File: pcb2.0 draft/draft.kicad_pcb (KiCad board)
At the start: 2 copper layers, 13 parts, among them J3 Conn_01x04, J4 Conn_01x04, J5 Conn_01x04, U2 LM2576HVS-5, U3 LM2576HVS-3.3

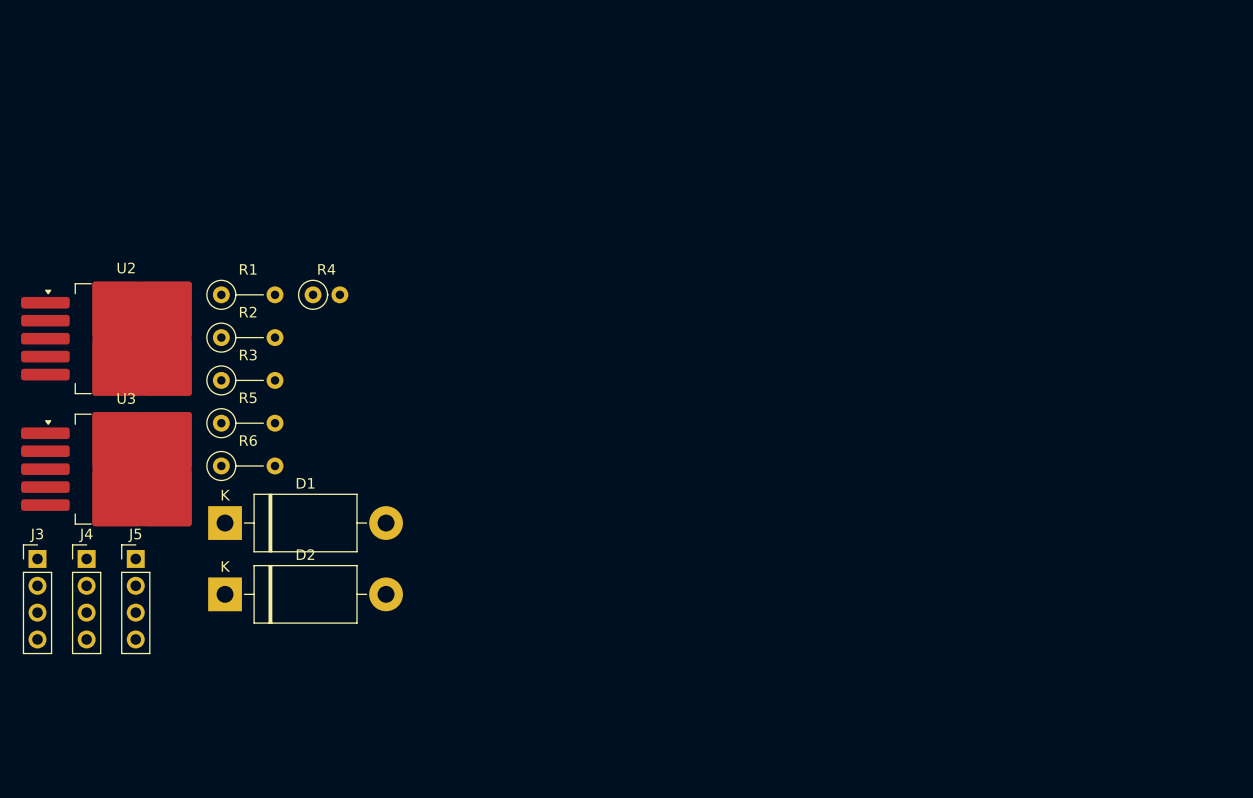
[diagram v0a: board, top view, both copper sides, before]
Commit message: completed pcb layout
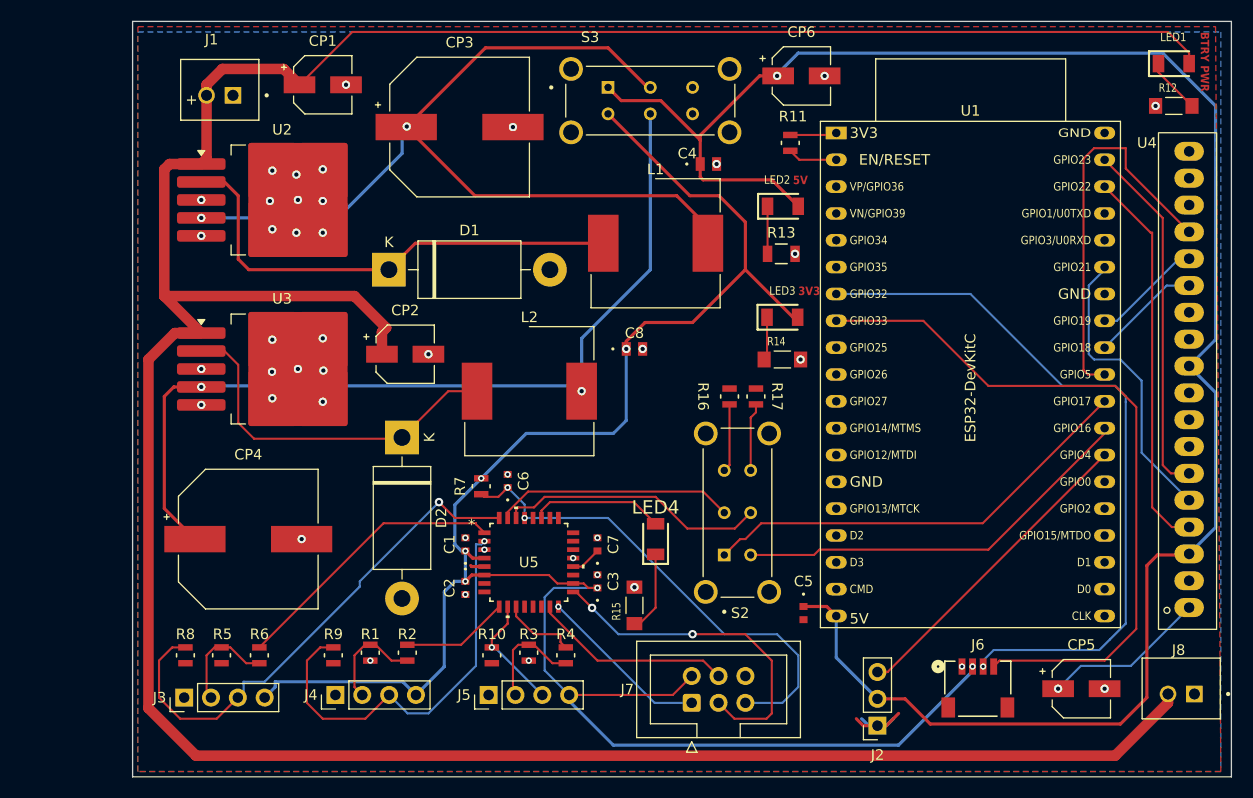
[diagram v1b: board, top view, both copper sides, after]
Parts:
- added C1: 0.1uF, cap_murata_0603:G-188_MUR-L, F.Cu at (137.0, 97.0)
- added C2: 0.1uF, cap_murata_0603:G-188_MUR-L, F.Cu at (137.0, 101.1)
- added C3: 0.1uF, cap_murata_0603:G-188_MUR-L, F.Cu at (149.5, 100.5)
- added C4: 1uF, cap_murata_0805:CAP_GRM21_MUR-L, F.Cu at (160.0, 61.0)
- added C5: 0.1uF, cap_murata_0603:G-188_MUR-L, F.Cu at (169.0, 103.5)
- added C6: 0.1uF, cap_murata_0603:G-188_MUR-L, F.Cu at (141.0, 91.0)
- added C7: 0.1uF, cap_murata_0603:G-188_MUR-L, F.Cu at (149.5, 97.0)
- added C8: 1uF, cap_murata_0805:CAP_GRM21_MUR-L, F.Cu at (153.0, 78.5)
- added CP1: 100uF, WurthE:CP_Wurth_WCAP-PSLP-D5L5.5, F.Cu at (123.5, 53.5)
- added CP2: 100uF, WurthE:CP_Wurth_WCAP-PSLP-D5L5.5, F.Cu at (131.3, 79.0)
- added CP3: 1mF, WurthE:CP_Wurth_WCAP-ASLI-D12.5L14, F.Cu at (136.4, 57.5)
- added CP4: 1mF, WurthE:CP_Wurth_WCAP-ASLI-D12.5L14, F.Cu at (116.5, 96.5)
- added CP5: 100uF, WurthE:CP_Wurth_WCAP-PSLP-D5L5.5, F.Cu at (195.3, 110.7)
- added CP6: 10uF, WurthE:CP_Wurth_WCAP-PSLP-D5L5.8, F.Cu at (168.8, 52.7)
- added J1: BTRY IN, jst_xh:JST_B2B-XH-A, F.Cu at (113.8, 54.0)
- added J2: Servo Header, Connector_PinSocket_2.54mm:PinSocket_1x03_P2.54mm_Vertical, F.Cu at (176.0, 114.2)
- added J6: QUIIC, quiic_jst:CONN_SM04B-SRSS-TB_JST, F.Cu at (185.5, 110.7)
- added J7: AVR-ISP-6, Connector_IDC:IDC-Header_2x03_P2.54mm_Vertical, F.Cu at (158.4, 112.0)
- added J8: BTRY OUT, jst_xh:JST_B2B-XH-A, F.Cu at (204.8, 110.6)
- added L1: 100uH, WE-PD:L_Wurth_WE-PD-1245, F.Cu at (155.0, 68.5)
- added L2: 100uH, WE-PD:L_Wurth_WE-PD-1245, F.Cu at (143.1, 82.5)
- added LED1: EAST3215BA3, led_smd_1206:LEDC3215X110N, F.Cu at (204.1, 51.5)
- added LED2: EAST3215BA3, led_smd_1206:LEDC3215X110N, F.Cu at (167.1, 65.0)
- added LED3: EAST3215BA3, led_smd_1206:LEDC3215X110N, F.Cu at (167.0, 75.5)
- added LED4: EAST3215BA3, led_smd_1206:LEDC3215X110N, F.Cu at (155.0, 96.5)
- added R10: 10k, R_SMD:RES_CR0805_VEN-L, F.Cu at (139.5, 107.5)
- added R11: 10k, R_SMD:RES_CR0805_VEN-L, F.Cu at (167.8, 59.0)
- added R12: 1.2k, r_erj_1p2k:RES_ERJU08J122V, F.Cu at (204.1, 55.5)
- added R13: 620, R_ERJ_620_1206:RC1206N_PAN-L, F.Cu at (166.9, 69.5)
- added R14: 270, r_erj_270:RES_ERJU08J271V, F.Cu at (167.0, 79.5)
- added R15: 270, r_erj_270:RES_ERJU08J271V, F.Cu at (153.0, 102.8)
- added R16: 10k, R_SMD:RES_CR0805_VEN-L, F.Cu at (162.0, 83.0)
- added R17: 10k, R_SMD:RES_CR0805_VEN-L, F.Cu at (164.5, 83.0)
- added R7: 10k, R_SMD:RES_CR0805_VEN-L, F.Cu at (138.5, 91.5)
- added R8: 10k, R_SMD:RES_CR0805_VEN-L, F.Cu at (110.5, 107.5)
- added R9: 10k, R_SMD:RES_CR0805_VEN-L, F.Cu at (124.5, 107.5)
- added S2: EG2201B, switch_eg2201_dpdt:SW_EG2201B, F.Cu at (162.8, 94.0)
- added S3: EG2201B, switch_eg2201_dpdt:SW_EG2201B, F.Cu at (154.5, 55.0)
- added U1: ESP32-DevKitC, PCM_Espressif:ESP32-DevKitC, F.Cu at (172.1, 58.1)
- added U4: ~, polulu_MC33926_dual:polulu_MC33926_dual, F.Cu at (205.4, 102.9)
- added U5: ATMEGA328P-ANR, atmega328p-anr:32A_ATM-L, F.Cu at (143.0, 98.7)
- R1, R3, R6: footprint Resistor_THT:R_Axial_DIN0207_L6.3mm_D2.5mm_P5.08mm_Vertical -> R_SMD:RES_CR0805_VEN-L
- R2: value 2k -> 1k; footprint Resistor_THT:R_Axial_DIN0207_L6.3mm_D2.5mm_P5.08mm_Vertical -> R_SMD:RES_CR0805_VEN-L
- R4: footprint Resistor_THT:R_Axial_DIN0207_L6.3mm_D2.5mm_P2.54mm_Vertical -> R_SMD:RES_CR0805_VEN-L
- R5: value 1k -> 2k; footprint Resistor_THT:R_Axial_DIN0207_L6.3mm_D2.5mm_P5.08mm_Vertical -> R_SMD:RES_CR0805_VEN-L
- moved R4 41.7 mm to (146.5, 107.5), turned to 90 degrees
- moved R3 38.9 mm to (143.0, 107.3), turned to 90 degrees
- moved R1 36.7 mm to (128.0, 107.3), turned to 90 degrees
- moved J5 35.8 mm to (139.2, 111.3), turned to 90 degrees
- moved R2 34.6 mm to (131.5, 107.3), turned to 90 degrees
- moved D1 28.6 mm to (129.8, 71.0)
- moved J4 26.8 mm to (124.7, 111.3), turned to 90 degrees
- moved D2 22.4 mm to (131.0, 86.9), turned to -90 degrees
- moved R5 22.0 mm to (113.9, 107.5), turned to 90 degrees
- moved U2 19.7 mm to (119.7, 64.4)
- moved J3 19.1 mm to (110.4, 111.5), turned to 90 degrees
- moved R6 18.3 mm to (117.5, 107.5), turned to 90 degrees
- moved U3 17.5 mm to (119.7, 80.4)
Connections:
- net /19 renamed 3V3
- D1 pad 2: Net-(D1-A) -> GND
- D2 pad 2: Net-(D1-A) -> GND
- J3 pad 1: /GND -> GND
- J3 pad 3: /29 -> Net-(J3-Pin_3)
- J4 pad 1: /GND -> GND
- J4 pad 3: /31 -> Net-(J4-Pin_3)
- J5 pad 1: /GND -> GND
- J5 pad 3: /36 -> Net-(J5-Pin_3)
- R1 pad 1: /GND -> GND
- R1 pad 2: Net-(J3-Pin_2) -> Net-(J4-Pin_2)
- R2 pad 1: /GND -> Net-(J4-Pin_2)
- R2 pad 2: Net-(J4-Pin_2) -> Net-(U5-PD5)
- R3 pad 1: /GND -> GND
- R4 pad 1: Net-(J3-Pin_2) -> Net-(J5-Pin_2)
- R4 pad 2: /30 -> Net-(U5-PD7)
- R5 pad 1: Net-(J4-Pin_2) -> GND
- R5 pad 2: /33 -> Net-(J3-Pin_2)
- R6 pad 1: Net-(J5-Pin_2) -> Net-(J3-Pin_2)
- R6 pad 2: /37 -> Net-(U5-PD3)
- U2 pad 1: Net-(D1-A) -> BTRY
- U2 pad 3: Net-(D1-A) -> GND
- U2 pad 4: Net-(U2-FB) -> 5V0
- U2 pad 5: Net-(D1-A) -> GND
- U3 pad 1: Net-(D1-A) -> BTRY
- U3 pad 3: Net-(D1-A) -> GND
- U3 pad 4: Net-(J2-Pin_1) -> 3V30
- U3 pad 5: Net-(D1-A) -> GND
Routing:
- net BTRY: track 0.00 -> 291.7 mm
- net 3V3: track 0.00 -> 193.7 mm, vias 0 -> 6
- net 5V: track 0.00 -> 182.3 mm, vias 0 -> 1
- net 5V0: track 0.00 -> 86.3 mm, vias 0 -> 2
- net 3V30: track 0.00 -> 83.8 mm, vias 0 -> 2
- net SDA: track 0.00 -> 68.4 mm, vias 0 -> 1
- net SCL: track 0.00 -> 67.8 mm
- net Net-(J3-Pin_3): track 0.00 -> 50.1 mm, vias 0 -> 1
- net RST: track 0.00 -> 46.4 mm, vias 0 -> 2
- net Net-(D1-K): track 0.00 -> 46.0 mm
- net Net-(U1-GPIO17): track 0.00 -> 42.0 mm
- net Net-(J4-Pin_3): track 0.00 -> 39.6 mm, vias 0 -> 1
- net Net-(U1-GPIO16): track 0.00 -> 38.8 mm
- net Net-(U1-GPIO5): track 0.00 -> 37.0 mm
- net Net-(U1-GPIO22): track 0.00 -> 36.6 mm
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- added copper zone on B.Cu, net GND
- added copper zone on F.Cu, net GND
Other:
- board outline added: 104 x 71.5 mm
- board text added: "+"
- board text added: "3V3"
- board text added: "5V"
- board text added: "BTRY PWR"

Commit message: broke out code into header files
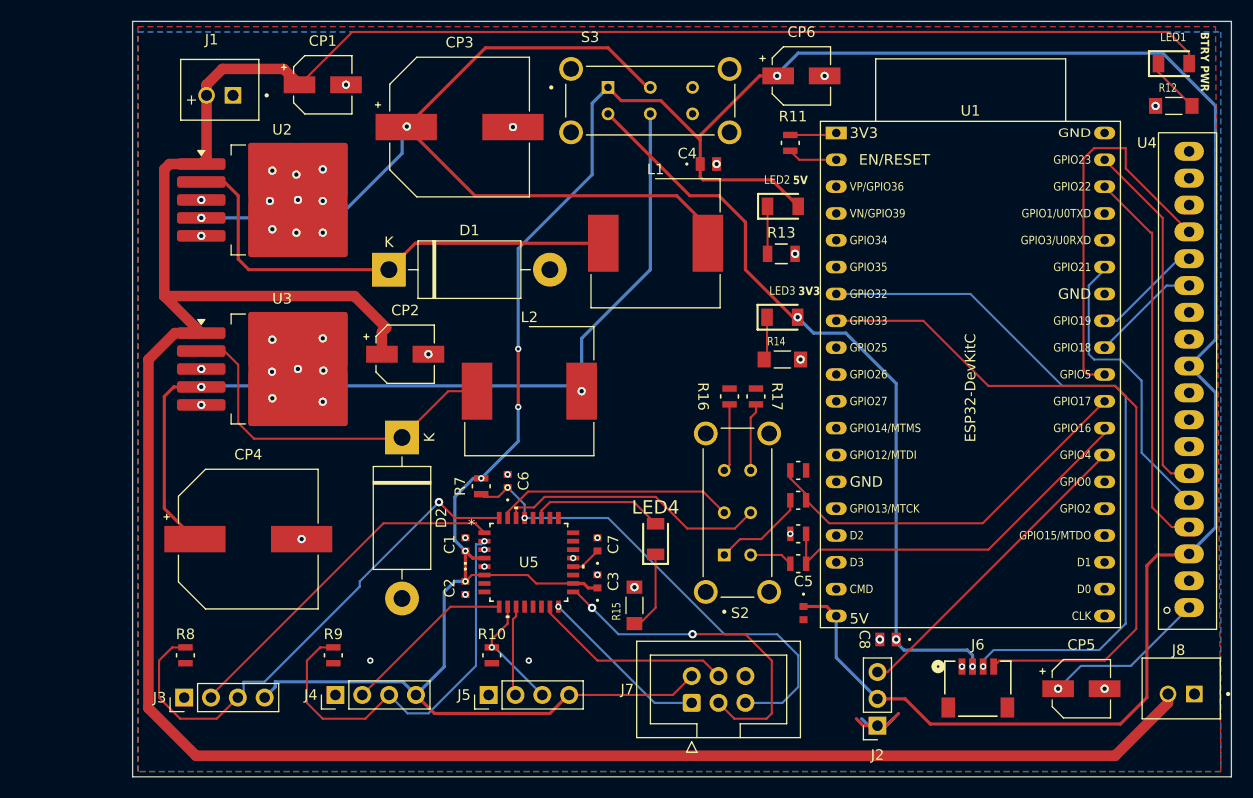
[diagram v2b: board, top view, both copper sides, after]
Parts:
- removed R3: 2k, R_SMD:RES_CR0805_VEN-L
- removed R4: 1k, R_SMD:RES_CR0805_VEN-L
- moved R5 57.3 mm to (168.5, 90.0), turned to 0 degrees
- moved R6 53.1 mm to (168.5, 92.8), turned to 0 degrees
- moved R1 42.0 mm to (168.5, 96.0), turned to 0 degrees
- moved R2 37.9 mm to (168.5, 98.8), turned to 0 degrees
- moved C8 36.5 mm to (177.0, 106.0), turned to 180 degrees
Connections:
- C1 pad 1: 3V3 -> 5V
- C2 pad 1: 3V3 -> 5V
- C3 pad 1: 3V3 -> 5V
- J3 pad 4: 3V3 -> 5V
- J4 pad 4: 3V3 -> 5V
- J5 pad 4: 3V3 -> 5V
- J7 pad 2: 3V3 -> 5V
- R1 pad 2: Net-(J4-Pin_2) -> Net-(U1-GPIO16)
- R2 pad 1: Net-(J4-Pin_2) -> Net-(R2-Pad1)
- R2 pad 2: Net-(U5-PD5) -> Net-(U1-GPIO16)
- R5 pad 1: GND -> Net-(U1-GPIO17)
- R5 pad 2: Net-(J3-Pin_2) -> GND
- R6 pad 1: Net-(J3-Pin_2) -> Net-(R6-Pad1)
- R6 pad 2: Net-(U5-PD3) -> Net-(U1-GPIO17)
- R7 pad 2: 3V3 -> 5V
- S2 pad 1: Net-(U1-GPIO17) -> Net-(R6-Pad1)
- S2 pad 4: Net-(U1-GPIO16) -> Net-(R2-Pad1)
- U5 pad 1: Net-(U5-PD3) -> Net-(J3-Pin_2)
- U5 pad 11: Net-(U5-PD7) -> Net-(J5-Pin_2)
- U5 pad 18: 3V3 -> 5V
- U5 pad 4: 3V3 -> 5V
- U5 pad 6: 3V3 -> 5V
- U5 pad 9: Net-(U5-PD5) -> Net-(J4-Pin_2)
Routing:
- net 5V: track 182.3 -> 309.2 mm, vias 1 -> 6
- net 3V3: track 193.7 -> 74.2 mm, vias 6 -> 3
- net Net-(U5-PD3): track 26.6 -> 0.00 mm
- net Net-(J3-Pin_2): track 10.1 -> 33.2 mm
- net Net-(U5-PD5): track 10.2 -> 0.00 mm
- net Net-(R6-Pad1): track 0.00 -> 8.93 mm
- net Net-(U5-PD7): track 7.26 -> 0.00 mm
- net Net-(J4-Pin_2): track 10.1 -> 16.4 mm
- net Net-(U1-GPIO17): track 42.0 -> 37.4 mm
- net Net-(R2-Pad1): track 0.00 -> 4.09 mm
- net Net-(U1-GPIO16): track 38.8 -> 36.7 mm
- net Net-(J5-Pin_2): track 10.3 -> 8.58 mm
- net GND: track 9.64 -> 8.30 mm, vias 42 -> 44
